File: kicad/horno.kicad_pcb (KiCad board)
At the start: 2 copper layers, 100.1 x 100.1 mm, 51 parts, among them P1 LPC1769, P10 Alimentación, P3 Termocupla, P4 TRIAC, P5 24V, P6 Motor, P7 Pantalla, P8 UART, P9 GPIO, Q1 BC547, SW1 RST, U1 OP07, U2 OP07, U3 LTC1050, U4 OP07, U5 L293D, U6 LM35

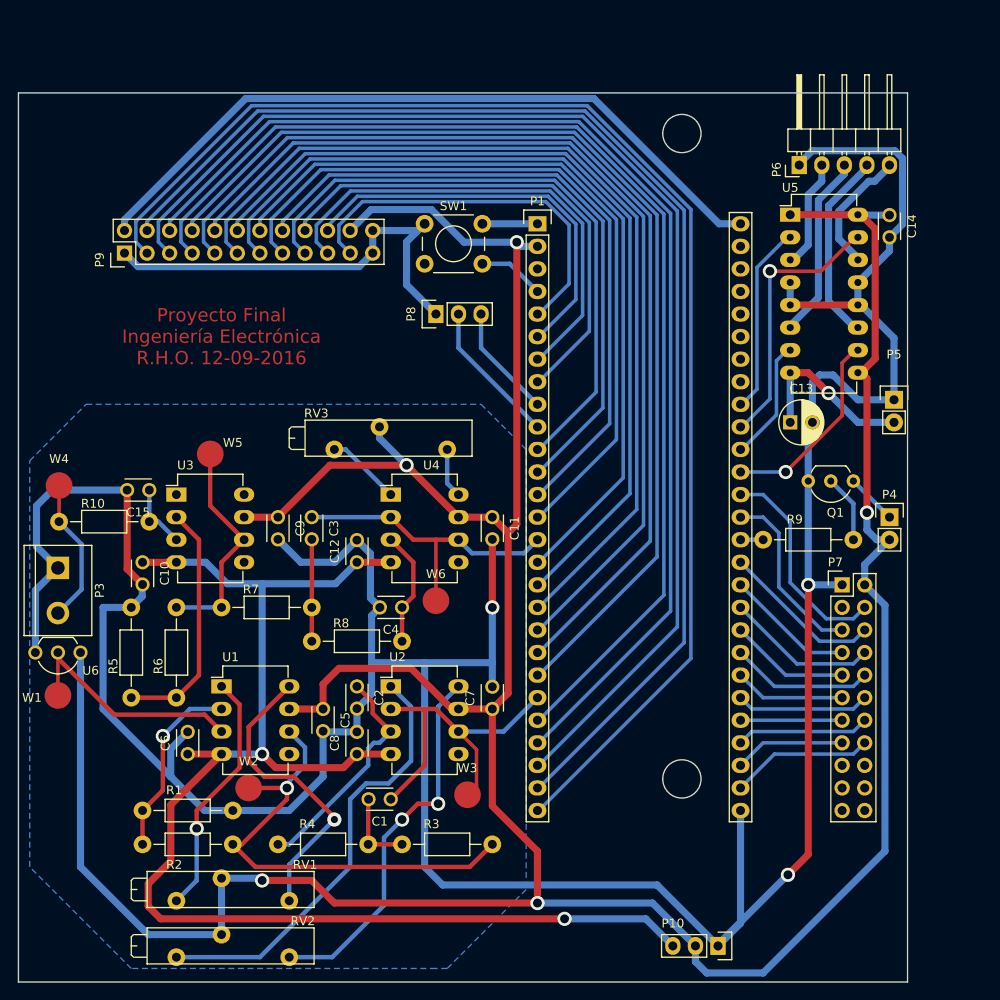
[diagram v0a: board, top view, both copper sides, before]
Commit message: corregir la posición de las etiquetas de los componentes en el pcb
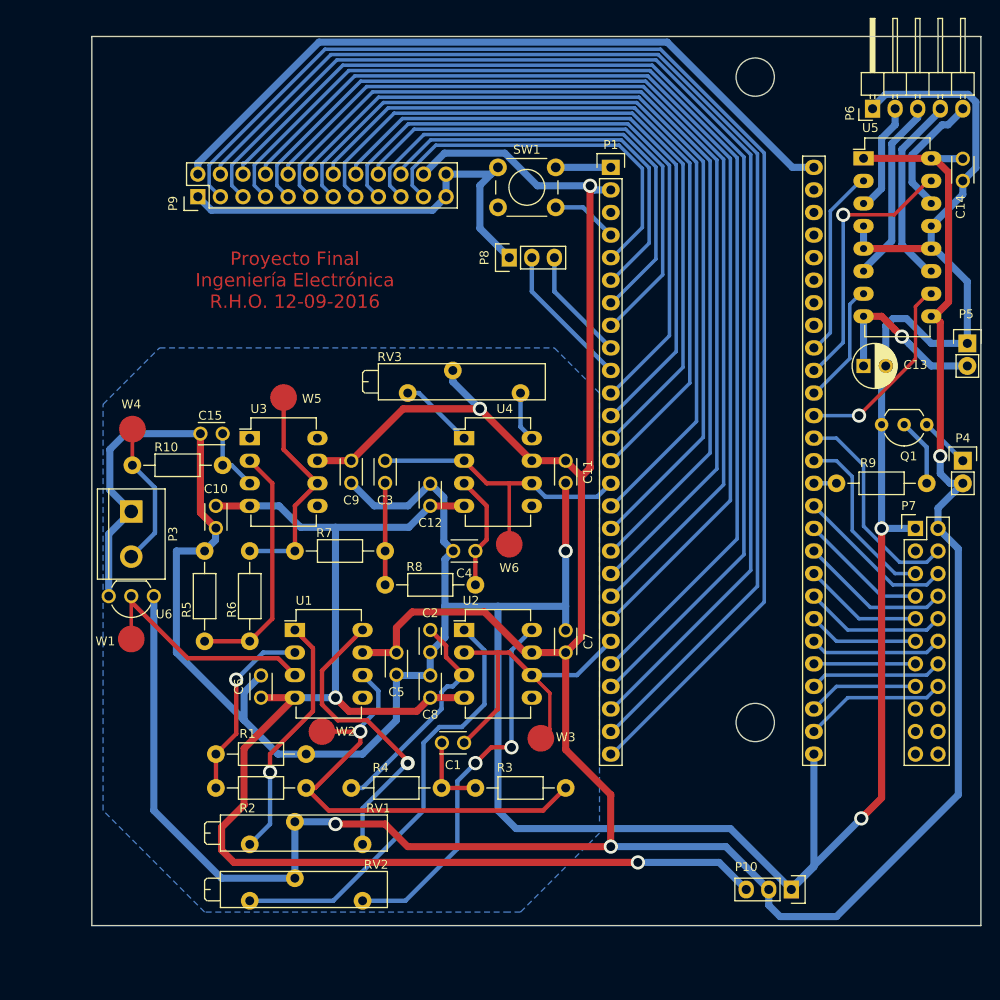
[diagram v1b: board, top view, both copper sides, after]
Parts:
- moved C11 10.4 mm to (148.0, 87.6)
- moved C7 10.4 mm to (148.0, 109.2)
- moved C12 10.4 mm to (132.7, 92.7)
- moved C3 10.4 mm to (127.6, 87.6)
- moved C6 10.4 mm to (113.7, 114.3)
- moved C8 10.4 mm to (132.7, 114.3)
- moved C9 10.4 mm to (123.8, 87.6)
- moved R2 10.4 mm to (118.7, 124.5)
- moved R4 10.4 mm to (123.8, 124.5)
- moved P10 10.4 mm to (173.4, 135.9)
- moved C2 10.4 mm to (132.7, 106.7)
- moved R7 10.4 mm to (127.6, 97.8)
- moved C1 10.4 mm to (136.5, 119.4)
- moved C10 10.4 mm to (108.6, 92.7)
- moved C15 10.4 mm to (109.3, 84.6)
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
